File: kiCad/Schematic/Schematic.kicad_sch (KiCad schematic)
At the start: 2 parts, among them J1 BAT, J2 Switch

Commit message: Day 1 -- Schematic - Added componednts
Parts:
- added J3: MPU 6050, symbol Connector_Generic:Conn_01x08
- added J4: ESP 32, symbol Connector_Generic:Conn_02x15_Counter_Clockwise
- added J5: UltraSonic Sensor, symbol Connector_Generic:Conn_01x04
- added J6: Conn_01x08, footprints:L298N-module-43x43mm, symbol Connector_Generic:Conn_01x08
- added M1, M2: Stepper_Motor_bipolar, symbol Motor:Stepper_Motor_bipolar
- J1: footprint (none) -> Button_Switch_THT:SW_E-Switch_EG1224_SPDT_Angled
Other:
- moved on the sheet: J1

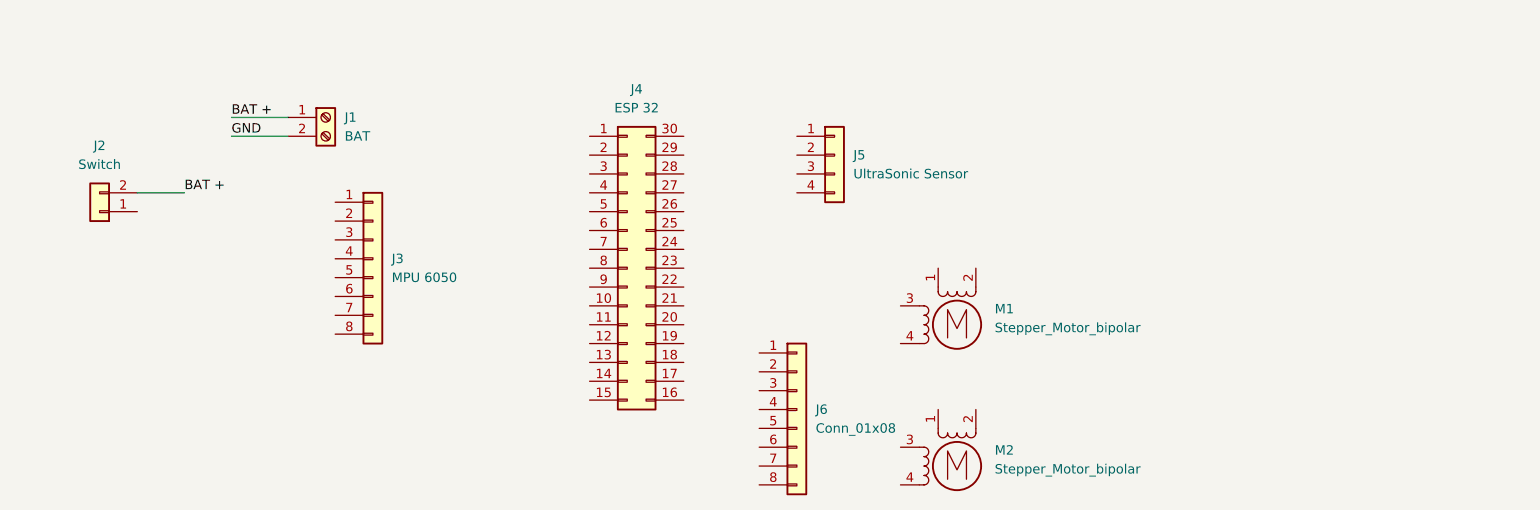
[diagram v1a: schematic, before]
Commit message: Day 1 -- Schematic - Added components
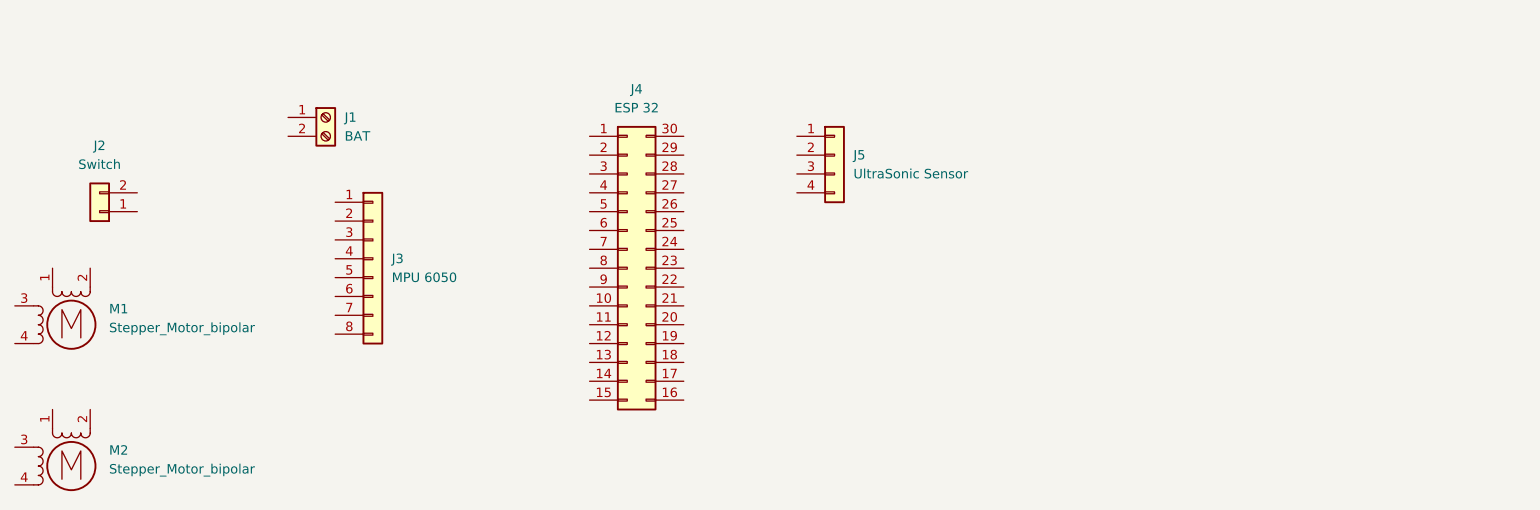
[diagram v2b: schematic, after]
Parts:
- removed J6: Conn_01x08, footprints:L298N-module-43x43mm, symbol Connector_Generic:Conn_01x08
- J1: footprint Button_Switch_THT:SW_E-Switch_EG1224_SPDT_Angled -> (none)
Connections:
- net BAT +: no longer names the net of J1.1 (Pin_1)
- net BAT +: no longer J2.2 (Pin_2)
- net GND: no longer names the net of J1.2 (Pin_2)
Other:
- moved on the sheet: M1, M2
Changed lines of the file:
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@@
 		(date "2026-07-02")
-	)
-	(wire
-		(pts
-			(xy 43.18 53.34) (xy 49.53 53.34)
-		)
-		(stroke
-			(width 0)
-			(type default)
-		)
-	)
-	(wire
-		(pts
-			(xy 55.88 45.72) (xy 63.5 45.72)
-		)
-		(stroke
-			(width 0)
-			(type default)
-		)
-	)
-	(wire
-		(pts
-			(xy 55.88 43.18) (xy 63.5 43.18)
-		)
-		(stroke
-			(width 0)
-			(type default)
-		)
-	)
-	(label "GND"
-		(at 55.88 45.72 0)
-		(effects
-			(font
-				(size 1.27 1.27)
-			)
-			(justify left bottom)
-		)
-	)
-	(label "BAT +"
-		(at 49.53 53.34 0)
-		(effects
-			(font
-				(size 1.27 1.27)
-			)
-			(justify left bottom)
-		)
-	)
-	(label "BAT +"
-		(at 55.88 43.18 0)
-		(effects
-			(font
-				(size 1.27 1.27)
-			)
-			(justify left bottom)
-		)
 	)
 	(symbol
@@
 			)
 		)
-		(property "Footprint" "Button_Switch_THT:SW_E-Switch_EG1224_SPDT_Angled"
+		(property "Footprint" ""
 			(at 68.58 43.18 0)
 			(hide yes)
@@
 	(symbol
 		(lib_id "Motor:Stepper_Motor_bipolar")
-		(at 153.67 90.17 0)
+		(at 34.29 90.17 0)
 		(unit 1)
 		(body_style 1)
@@
 		(fields_autoplaced yes)
 		(property "Reference" "M2"
-			(at 158.75 88.049 0)
+			(at 39.37 88.049 0)
 			(show_name no)
 			(do_not_autoplace no)
@@
 		)
 		(property "Value" "Stepper_Motor_bipolar"
-			(at 158.75 90.589 0)
-			(show_name no)
-			(do_not_autoplace no)
-			(effects
-				(font
-					(size 1.27 1.27)
-				)
-				(justify left)
-			)
-		)
-		(property "Footprint" ""
-			(at 153.924 90.424 0)
+			(at 39.37 90.589 0)
+			(show_name no)
+			(do_not_autoplace no)
+			(effects
+				(font
+					(size 1.27 1.27)
+				)
+				(justify left)
+			)
+		)
+		(property "Footprint" ""
+			(at 34.544 90.424 0)
 			(hide yes)
 			(show_name no)
@@
 		)
 		(property "Datasheet" "http://www.infineon.com/dgdl/Application-Note-TLE8110EE_driving_UniPolarStepperMotor_V1.1.pdf?fileId=db3a30431be39b97011be5d0aa0a00b0"
-			(at 153.924 90.424 0)
+			(at 34.544 90.424 0)
 			(hide yes)
 			(show_name no)
@@
 		)
 		(property "Description" "4-wire bipolar stepper motor"
-			(at 153.67 90.17 0)
+			(at 34.29 90.17 0)
 			(hide yes)
 			(show_name no)
@@
 	)
 	(symbol
-		(lib_id "Connector_Generic:Conn_01x08")
-		(at 132.08 82.55 0)
-		(unit 1)
-		(body_style 1)
-		(exclude_from_sim no)
-		(in_bom yes)
-		(on_board yes)
-		(in_pos_files yes)
-		(dnp no)
-		(fields_autoplaced yes)
-		(property "Reference" "J6"
-			(at 134.62 82.5499 0)
-			(show_name no)
-			(do_not_autoplace no)
-			(effects
-				(font
-					(size 1.27 1.27)
-				)
-				(justify left)
-			)
-		)
-		(property "Value" "Conn_01x08"
-			(at 134.62 85.0899 0)
-			(show_name no)
-			(do_not_autoplace no)
-			(effects
-				(font
-					(size 1.27 1.27)
-				)
-				(justify left)
-			)
-		)
-		(property "Footprint" "footprints:L298N-module-43x43mm"
-			(at 132.08 82.55 0)
-			(hide yes)
-			(show_name no)
-			(do_not_autoplace no)
-			(effects
-				(font
-					(size 1.27 1.27)
-				)
-			)
-		)
-		(property "Datasheet" ""
-			(at 132.08 82.55 0)
-			(hide yes)
-			(show_name no)
-			(do_not_autoplace no)
-			(effects
-				(font
-					(size 1.27 1.27)
-				)
-			)
-		)
-		(property "Description" "Generic connector, single row, 01x08, script generated (kicad-library-utils/schlib/autogen/connector/)"
-			(at 132.08 82.55 0)
-			(hide yes)
-			(show_name no)
-			(do_not_autoplace no)
-			(effects
-				(font
-					(size 1.27 1.27)
-				)
-			)
-		)
-		(pin "2"
-		)
-		(pin "8"
-		)
-		(pin "3"
-		)
-		(pin "6"
-		)
-		(pin "1"
-		)
-		(pin "4"
-		)
-		(pin "5"
-		)
-		(pin "7"
-		)
-		(instances
-			(project "Schematic"
-				(path "/bef6098d-5d9c-4874-b9bc-41576a37c7a0"
-					(reference "J6")
-					(unit 1)
-				)
-			)
-		)
-	)
-	(symbol
 		(lib_id "Motor:Stepper_Motor_bipolar")
-		(at 153.67 71.12 0)
+		(at 34.29 71.12 0)
 		(unit 1)
 		(body_style 1)
@@
 		(fields_autoplaced yes)
 		(property "Reference" "M1"
-			(at 158.75 68.999 0)
+			(at 39.37 68.999 0)
 			(show_name no)
 			(do_not_autoplace no)
@@
 		)
 		(property "Value" "Stepper_Motor_bipolar"
-			(at 158.75 71.539 0)
-			(show_name no)
-			(do_not_autoplace no)
-			(effects
-				(font
-					(size 1.27 1.27)
-				)
-				(justify left)
-			)
-		)
-		(property "Footprint" ""
-			(at 153.924 71.374 0)
+			(at 39.37 71.539 0)
+			(show_name no)
+			(do_not_autoplace no)
+			(effects
+				(font
+					(size 1.27 1.27)
+				)
+				(justify left)
+			)
+		)
+		(property "Footprint" ""
+			(at 34.544 71.374 0)
 			(hide yes)
 			(show_name no)
@@
 		)
 		(property "Datasheet" "http://www.infineon.com/dgdl/Application-Note-TLE8110EE_driving_UniPolarStepperMotor_V1.1.pdf?fileId=db3a30431be39b97011be5d0aa0a00b0"
-			(at 153.924 71.374 0)
+			(at 34.544 71.374 0)
 			(hide yes)
 			(show_name no)
@@
 		)
 		(property "Description" "4-wire bipolar stepper motor"
-			(at 153.67 71.12 0)
-			(hide yes)
-			(show_name no)
+			(at 34.29 71.12 0)
+			(hide yes)
+			(show_name no)
